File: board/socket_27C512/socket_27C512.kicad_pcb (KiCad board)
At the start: 2 copper layers, 17.8 x 35.6 mm, 2 parts

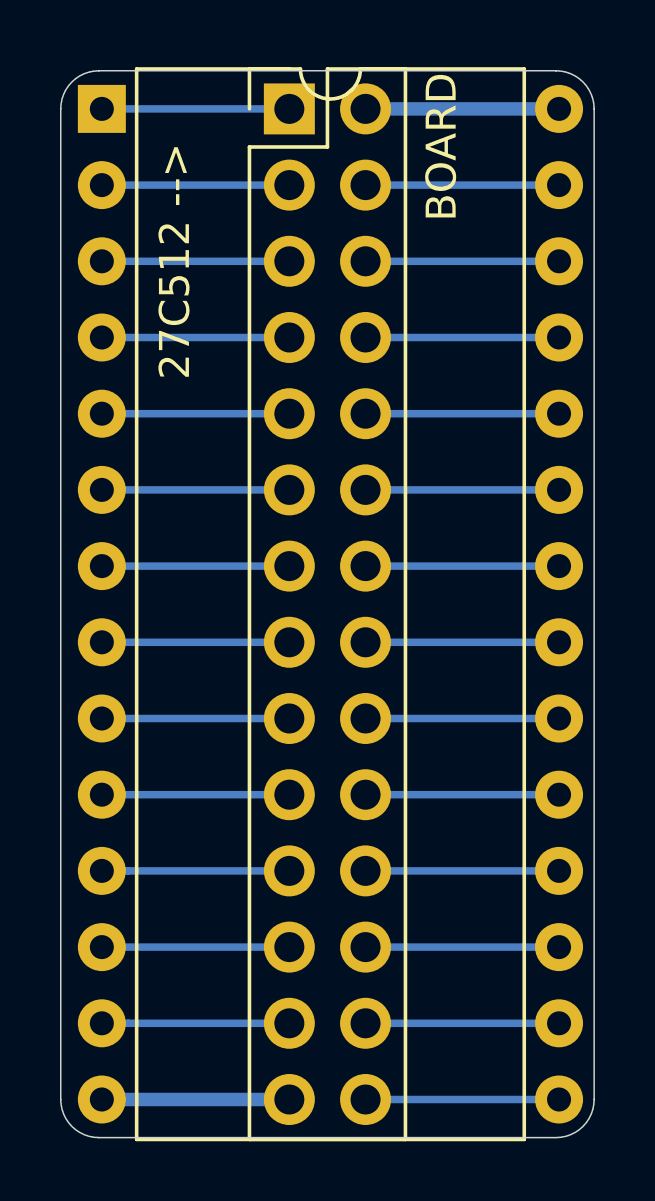
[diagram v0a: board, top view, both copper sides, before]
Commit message: Add 27C400/16 socket
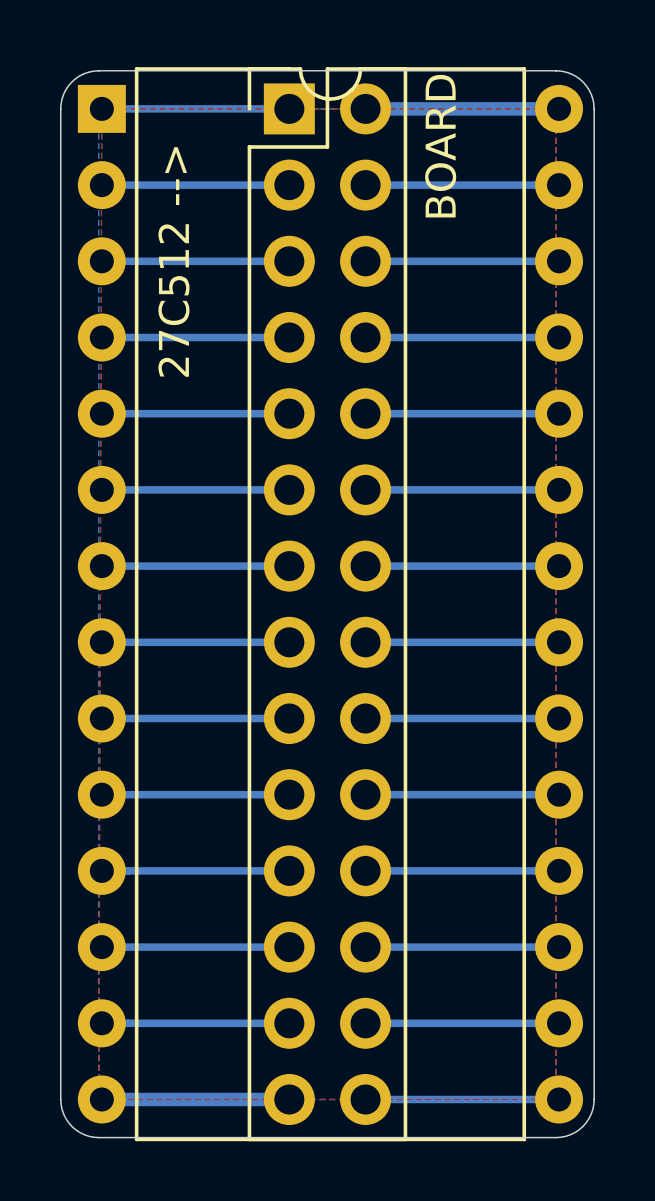
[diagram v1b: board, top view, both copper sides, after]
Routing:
- added copper zone on B.Cu, net GND
- added copper zone on F.Cu, net GND
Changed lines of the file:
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@@
       (effects (font (size 1 1) (thickness 0.15)))
     )
+    (fp_line (start 16.3 -1.55) (end -1.05 -1.55) (layer F.CrtYd) (width 0.05))
+    (fp_line (start 16.3 34.55) (end 16.3 -1.55) (layer F.CrtYd) (width 0.05))
+    (fp_line (start -1.05 34.55) (end 16.3 34.55) (layer F.CrtYd) (width 0.05))
+    (fp_line (start -1.05 -1.55) (end -1.05 34.55) (layer F.CrtYd) (width 0.05))
+    (fp_line (start 14.08 -1.33) (end 8.62 -1.33) (layer F.SilkS) (width 0.12))
+    (fp_line (start 14.08 34.35) (end 14.08 -1.33) (layer F.SilkS) (width 0.12))
+    (fp_line (start 1.16 34.35) (end 14.08 34.35) (layer F.SilkS) (width 0.12))
+    (fp_line (start 1.16 -1.33) (end 1.16 34.35) (layer F.SilkS) (width 0.12))
+    (fp_line (start 6.62 -1.33) (end 1.16 -1.33) (layer F.SilkS) (width 0.12))
+    (fp_line (start 0.255 -0.27) (end 1.255 -1.27) (layer F.Fab) (width 0.1))
+    (fp_line (start 0.255 34.29) (end 0.255 -0.27) (layer F.Fab) (width 0.1))
+    (fp_line (start 14.985 34.29) (end 0.255 34.29) (layer F.Fab) (width 0.1))
+    (fp_line (start 14.985 -1.27) (end 14.985 34.29) (layer F.Fab) (width 0.1))
+    (fp_line (start 1.255 -1.27) (end 14.985 -1.27) (layer F.Fab) (width 0.1))
     (fp_text user %R (at 7.62 16.51) (layer F.Fab)
       (effects (font (size 1 1) (thickness 0.15)))
     )
     (fp_arc (start 7.62 -1.33) (end 6.62 -1.33) (angle -180) (layer F.SilkS) (width 0.12))
-    (fp_line (start 1.255 -1.27) (end 14.985 -1.27) (layer F.Fab) (width 0.1))
-    (fp_line (start 14.985 -1.27) (end 14.985 34.29) (layer F.Fab) (width 0.1))
-    (fp_line (start 14.985 34.29) (end 0.255 34.29) (layer F.Fab) (width 0.1))
-    (fp_line (start 0.255 34.29) (end 0.255 -0.27) (layer F.Fab) (width 0.1))
-    (fp_line (start 0.255 -0.27) (end 1.255 -1.27) (layer F.Fab) (width 0.1))
-    (fp_line (start 6.62 -1.33) (end 1.16 -1.33) (layer F.SilkS) (width 0.12))
-    (fp_line (start 1.16 -1.33) (end 1.16 34.35) (layer F.SilkS) (width 0.12))
-    (fp_line (start 1.16 34.35) (end 14.08 34.35) (layer F.SilkS) (width 0.12))
-    (fp_line (start 14.08 34.35) (end 14.08 -1.33) (layer F.SilkS) (width 0.12))
-    (fp_line (start 14.08 -1.33) (end 8.62 -1.33) (layer F.SilkS) (width 0.12))
-    (fp_line (start -1.05 -1.55) (end -1.05 34.55) (layer F.CrtYd) (width 0.05))
-    (fp_line (start -1.05 34.55) (end 16.3 34.55) (layer F.CrtYd) (width 0.05))
-    (fp_line (start 16.3 34.55) (end 16.3 -1.55) (layer F.CrtYd) (width 0.05))
-    (fp_line (start 16.3 -1.55) (end -1.05 -1.55) (layer F.CrtYd) (width 0.05))
     (pad 28 thru_hole oval (at 15.24 0) (size 1.6 1.6) (drill 0.8) (layers *.Cu *.Mask)
       (net 27 /VCC_EXT))
@@
       (effects (font (size 1 1) (thickness 0.15)))
     )
+    (fp_line (start 4.35 -1.8) (end -1.8 -1.8) (layer F.CrtYd) (width 0.05))
+    (fp_line (start 4.35 34.8) (end 4.35 -1.8) (layer F.CrtYd) (width 0.05))
+    (fp_line (start -1.8 34.8) (end 4.35 34.8) (layer F.CrtYd) (width 0.05))
+    (fp_line (start -1.8 -1.8) (end -1.8 34.8) (layer F.CrtYd) (width 0.05))
+    (fp_line (start -1.33 -1.33) (end 0 -1.33) (layer F.SilkS) (width 0.12))
+    (fp_line (start -1.33 0) (end -1.33 -1.33) (layer F.SilkS) (width 0.12))
+    (fp_line (start 1.27 -1.33) (end 3.87 -1.33) (layer F.SilkS) (width 0.12))
+    (fp_line (start 1.27 1.27) (end 1.27 -1.33) (layer F.SilkS) (width 0.12))
+    (fp_line (start -1.33 1.27) (end 1.27 1.27) (layer F.SilkS) (width 0.12))
+    (fp_line (start 3.87 -1.33) (end 3.87 34.35) (layer F.SilkS) (width 0.12))
+    (fp_line (start -1.33 1.27) (end -1.33 34.35) (layer F.SilkS) (width 0.12))
+    (fp_line (start -1.33 34.35) (end 3.87 34.35) (layer F.SilkS) (width 0.12))
+    (fp_line (start -1.27 0) (end 0 -1.27) (layer F.Fab) (width 0.1))
+    (fp_line (start -1.27 34.29) (end -1.27 0) (layer F.Fab) (width 0.1))
+    (fp_line (start 3.81 34.29) (end -1.27 34.29) (layer F.Fab) (width 0.1))
+    (fp_line (start 3.81 -1.27) (end 3.81 34.29) (layer F.Fab) (width 0.1))
+    (fp_line (start 0 -1.27) (end 3.81 -1.27) (layer F.Fab) (width 0.1))
     (fp_text user %R (at 1.27 16.51 90) (layer F.Fab)
       (effects (font (size 1 1) (thickness 0.15)))
     )
-    (fp_line (start 0 -1.27) (end 3.81 -1.27) (layer F.Fab) (width 0.1))
-    (fp_line (start 3.81 -1.27) (end 3.81 34.29) (layer F.Fab) (width 0.1))
-    (fp_line (start 3.81 34.29) (end -1.27 34.29) (layer F.Fab) (width 0.1))
-    (fp_line (start -1.27 34.29) (end -1.27 0) (layer F.Fab) (width 0.1))
-    (fp_line (start -1.27 0) (end 0 -1.27) (layer F.Fab) (width 0.1))
-    (fp_line (start -1.33 34.35) (end 3.87 34.35) (layer F.SilkS) (width 0.12))
-    (fp_line (start -1.33 1.27) (end -1.33 34.35) (layer F.SilkS) (width 0.12))
-    (fp_line (start 3.87 -1.33) (end 3.87 34.35) (layer F.SilkS) (width 0.12))
-    (fp_line (start -1.33 1.27) (end 1.27 1.27) (layer F.SilkS) (width 0.12))
-    (fp_line (start 1.27 1.27) (end 1.27 -1.33) (layer F.SilkS) (width 0.12))
-    (fp_line (start 1.27 -1.33) (end 3.87 -1.33) (layer F.SilkS) (width 0.12))
-    (fp_line (start -1.33 0) (end -1.33 -1.33) (layer F.SilkS) (width 0.12))
-    (fp_line (start -1.33 -1.33) (end 0 -1.33) (layer F.SilkS) (width 0.12))
-    (fp_line (start -1.8 -1.8) (end -1.8 34.8) (layer F.CrtYd) (width 0.05))
-    (fp_line (start -1.8 34.8) (end 4.35 34.8) (layer F.CrtYd) (width 0.05))
-    (fp_line (start 4.35 34.8) (end 4.35 -1.8) (layer F.CrtYd) (width 0.05))
-    (fp_line (start 4.35 -1.8) (end -1.8 -1.8) (layer F.CrtYd) (width 0.05))
     (pad 28 thru_hole oval (at 2.54 33.02) (size 1.7 1.7) (drill 1) (layers *.Cu *.Mask)
       (net 1 /D3))
@@
   (segment (start 134.72 73.66) (end 128.27 73.66) (width 0.45) (layer B.Cu) (net 27))
   (segment (start 125.73 73.66) (end 119.48 73.66) (width 0.25) (layer B.Cu) (net 28))
+  (zone (net 2) (net_name GND) (layer B.Cu) (hatch edge 0.508)
+    (connect_pads (clearance 0.508))
+    (min_thickness 0.254)
+    (fill yes (arc_segments 32) (thermal_gap 0.508) (thermal_bridge_width 0.508))
+    (polygon
+      (pts
+        (xy 134.62 106.68) (xy 119.38 106.68) (xy 119.38 73.66) (xy 134.62 73.66)
+      )
+    )
+  )
+  (zone (net 2) (net_name GND) (layer F.Cu) (hatch edge 0.508)
+    (connect_pads (clearance 0.508))
+    (min_thickness 0.254)
+    (fill yes (arc_segments 32) (thermal_gap 0.508) (thermal_bridge_width 0.508))
+    (polygon
+      (pts
+        (xy 134.62 106.68) (xy 119.38 106.68) (xy 119.48 73.66) (xy 134.62 73.66)
+      )
+    )
+  )
 )
